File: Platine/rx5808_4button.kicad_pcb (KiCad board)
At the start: 2 copper layers, 50.5 x 29.5 mm, 52 parts, among them IC1 ATMEGA328-A, P1 CONN_01X02, P2 CONN_01X05, P5 BNC, P6 CONN_01X04, P7 CONN_02X05, U1 TPS62160, U2 RX5808, U3 sn74lvc1g3157, U4 MCPL3-BC-V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

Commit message: BOM für beide platinen des kompletten moduls dazugefügt
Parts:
- SMA_E1: footprint PhilippsFootprints:SMA_EDGE_small -> PhilippsFootprints:SMA_EDGE_Johnson_142-0701-801
- moved SMA_E1 2.20 mm to (106.7, 103.7)
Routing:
- net GND: track 187.9 -> 184.5 mm
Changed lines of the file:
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@@
     (thickness 1.6)
     (drawings 16)
-    (tracks 660)
+    (tracks 658)
     (zones 0)
     (modules 52)
@@
   )
   (setup
-    (last_trace_width 0.25)
+    (last_trace_width 0.254)
     (user_trace_width 0.2032)
     (user_trace_width 0.254)
@@
     (visible_elements FFFEFF39)
     (pcbplotparams
-      (layerselection 0x014f0_ffffffff)
+      (layerselection 0x010f0_ffffffff)
       (usegerberextensions true)
       (excludeedgelayer true)
@@
       (plotinvisibletext false)
       (padsonsilk false)
-      (subtractmaskfromsilk false)
+      (subtractmaskfromsilk true)
       (outputformat 1)
       (mirror false)
@@
     )
   )
-  (module PhilippsFootprints:SMA_EDGE_small (layer F.Cu)
-    (at 106.7 105.9 180)
-    (fp_text reference SMA_E1 (at 0 0 180) (layer F.SilkS)
-      (effects (font (thickness 0.3048)))
-    )
-    (fp_text value SMA_EDGE (at 0 2.54 180) (layer F.SilkS) hide
-      (effects (font (thickness 0.3048)))
-    )
-    (fp_line (start -6.35 -2.5654) (end -6.35 5.0546) (layer F.SilkS) (width 0.381))
-    (fp_line (start -6.35 5.0546) (end 6.35 5.0546) (layer F.SilkS) (width 0.381))
-    (fp_line (start 6.35 5.0546) (end 6.35 -2.5654) (layer F.SilkS) (width 0.381))
-    (fp_line (start 6.35 -2.5654) (end -6.35 -2.5654) (layer F.SilkS) (width 0.381))
-    (pad 0 connect rect (at -8.8773 -1.89484 180) (size 4.572 1.524) (layers *.Cu F.Mask)
-      (net 2 GND))
-    (pad 1 connect trapezoid (at -6.858 1.27 180) (size 0.50038 1.39954) (rect_delta 0.59944 0 ) (layers B.Cu B.Mask)
-      (net 27 "Net-(SMA_E1-Pad1)"))
-    (pad 2 connect rect (at -8.8773 4.42976 180) (size 4.572 1.524) (layers *.Cu F.Mask)
-      (net 2 GND))
-    (pad 1 connect rect (at -9.144 1.27 180) (size 4.07162 1.99898) (layers B.Cu B.Mask)
-      (net 27 "Net-(SMA_E1-Pad1)") (clearance 0.5))
-    (model SMA_EDGE.wrl
-      (at (xyz -0.205 -0.05 -0.12))
-      (scale (xyz 1.3 1.3 1.3))
-      (rotate (xyz 270 0 180))
-    )
-  )
   (module NR3015:NR3015 (layer F.Cu)
     (at 129.4 117.6 90)
@@
     )
   )
+  (module PhilippsFootprints:SMA_EDGE_Johnson_142-0701-801 (layer F.Cu)
+    (at 106.7 103.7 180)
+    (fp_text reference SMA_E1 (at 0 -1.3 180) (layer F.SilkS)
+      (effects (font (thickness 0.3048)))
+    )
+    (fp_text value SMA_EDGE (at 0 1.24 180) (layer F.SilkS) hide
+      (effects (font (thickness 0.3048)))
+    )
+    (fp_line (start -6.2 -5.6) (end -6.3 -5.6) (layer F.SilkS) (width 0.15))
+    (fp_line (start -6.3 -5.6) (end -11.2 -5.6) (layer F.SilkS) (width 0.15))
+    (fp_line (start -11.2 -5.6) (end -11.2 5.6) (layer F.SilkS) (width 0.15))
+    (fp_line (start -11.2 5.6) (end -6.2 5.6) (layer F.SilkS) (width 0.15))
+    (fp_line (start -6.2 5.6) (end -6.2 -5.6) (layer F.SilkS) (width 0.15))
+    (fp_line (start -6.35 -3.8654) (end -6.35 3.7546) (layer F.SilkS) (width 0.381))
+    (fp_line (start -6.35 3.7546) (end 6.35 3.7546) (layer F.SilkS) (width 0.381))
+    (fp_line (start 6.35 3.7546) (end 6.35 -3.8654) (layer F.SilkS) (width 0.381))
+    (fp_line (start 6.35 -3.8654) (end -6.35 -3.8654) (layer F.SilkS) (width 0.381))
+    (pad 0 connect rect (at -8.9 -4.4 180) (size 4.572 2.413) (layers *.Mask B.Cu)
+      (net 2 GND))
+    (pad 1 connect trapezoid (at -6.858 -0.03 180) (size 0.50038 1.39954) (rect_delta 0.59944 0 ) (layers B.Cu B.Mask)
+      (net 27 "Net-(SMA_E1-Pad1)"))
+    (pad 2 connect rect (at -8.9 4.4 180) (size 4.572 2.413) (layers *.Mask B.Cu)
+      (net 2 GND))
+    (pad 1 connect rect (at -9.144 -0.03 180) (size 4.07162 2.2) (layers B.Cu B.Mask)
+      (net 27 "Net-(SMA_E1-Pad1)"))
+    (model SMA_EDGE.wrl
+      (at (xyz -0.205 -0.05 -0.12))
+      (scale (xyz 1.3 1.3 1.3))
+      (rotate (xyz 270 0 180))
+    )
+  )
   (gr_text 12V (at 118.7 116.8 90) (layer F.SilkS)
     (effects (font (size 1.5 1.5) (thickness 0.3)))
   )
-  (gr_text Antenne (at 119.7 104.7) (layer F.SilkS)
+  (gr_text Antenne (at 105.4 110.8) (layer F.SilkS)
     (effects (font (size 1.5 1.5) (thickness 0.3)))
   )
@@
   (segment (start 142.525 99.7) (end 141.61381 98.78881) (width 0.254) (layer F.Cu) (net 1) (status 10))
   (segment (start 142.55 99.7) (end 142.525 99.7) (width 0.254) (layer F.Cu) (net 1) (status 30))
+  (segment (start 121.26 107.17) (end 121.26 107.54) (width 1.016) (layer B.Cu) (net 2))
+  (segment (start 121.26 107.54) (end 120.7 108.1) (width 1.016) (layer B.Cu) (net 2))
+  (segment (start 120.7 108.1) (end 115.6 108.1) (width 1.016) (layer B.Cu) (net 2))
+  (segment (start 121.26 102.09) (end 121.26 100.96) (width 1.016) (layer B.Cu) (net 2))
+  (segment (start 119.6 99.3) (end 115.6 99.3) (width 1.016) (layer B.Cu) (net 2))
+  (segment (start 121.26 100.96) (end 119.6 99.3) (width 1.016) (layer B.Cu) (net 2))
   (segment (start 127.5 101.2) (end 127.5 99.84) (width 0.4064) (layer F.Cu) (net 2))
   (segment (start 127.5 99.84) (end 128.54 98.8) (width 0.4064) (layer F.Cu) (net 2))
-  (segment (start 115.5773 107.79484) (end 118.20516 107.79484) (width 0.254) (layer B.Cu) (net 2))
-  (segment (start 118.20516 107.79484) (end 118.32024 107.67976) (width 0.254) (layer B.Cu) (net 2))
-  (segment (start 115.5773 101.47024) (end 117.99008 101.47024) (width 0.254) (layer B.Cu) (net 2))
-  (segment (start 117.99008 101.47024) (end 118.10516 101.35516) (width 0.254) (layer B.Cu) (net 2))
   (segment (start 128.54 98.8) (end 130.08778 100.34778) (width 0.4064) (layer B.Cu) (net 2))
   (segment (start 130.08778 100.34778) (end 134.31774 100.34778) (width 0.4064) (layer B.Cu) (net 2))
@@
   (segment (start 144.3 117.74996) (end 144.3 120.4) (width 0.254) (layer F.Cu) (net 2) (status 30))
   (segment (start 144.3 120.4) (end 144.4 120.5) (width 0.254) (layer F.Cu) (net 2) (status 30))
-  (segment (start 115.6273 101.35516) (end 118.10516 101.35516) (width 1.016) (layer B.Cu) (net 2) (status 10))
-  (segment (start 118.84 102.09) (end 121.26 102.09) (width 1.016) (layer B.Cu) (net 2) (status 20))
-  (segment (start 118.10516 101.35516) (end 118.84 102.09) (width 1.016) (layer B.Cu) (net 2))
-  (segment (start 121.26 107.17) (end 118.83 107.17) (width 1.016) (layer B.Cu) (net 2) (status 10))
-  (segment (start 118.32024 107.67976) (end 115.6273 107.67976) (width 1.016) (layer B.Cu) (net 2) (status 20))
-  (segment (start 118.83 107.17) (end 118.32024 107.67976) (width 1.016) (layer B.Cu) (net 2))
   (segment (start 145.537717 117.023276) (end 147 118.485559) (width 0.254) (layer F.Cu) (net 2) (status 20))
   (segment (start 147 118.485559) (end 147 118.55) (width 0.254) (layer F.Cu) (net 2) (status 30))
@@
   (segment (start 127.05 120.6) (end 127.05 121.65) (width 0.254) (layer F.Cu) (net 26) (status 20))
   (segment (start 127 119.975) (end 127 120.55) (width 0.254) (layer F.Cu) (net 26) (status 10))
-  (segment (start 121.26 104.63) (end 115.844 104.63) (width 1.016) (layer B.Cu) (net 27))
-  (segment (start 115.844 104.63) (end 113.558 104.63) (width 0.254) (layer B.Cu) (net 27))
+  (segment (start 113.558 103.73) (end 115.844 103.73) (width 0.254) (layer B.Cu) (net 27))
+  (segment (start 121.26 104.63) (end 119.23 104.63) (width 1.016) (layer B.Cu) (net 27))
+  (segment (start 118.33 103.73) (end 115.844 103.73) (width 1.016) (layer B.Cu) (net 27))
+  (segment (start 119.23 104.63) (end 118.33 103.73) (width 1.016) (layer B.Cu) (net 27))
   (segment (start 121.16516 104.53516) (end 121.26 104.63) (width 0.254) (layer B.Cu) (net 27) (status 30))
   (segment (start 121.15 104.52) (end 121.26 104.63) (width 0.508) (layer B.Cu) (net 27) (status 30))

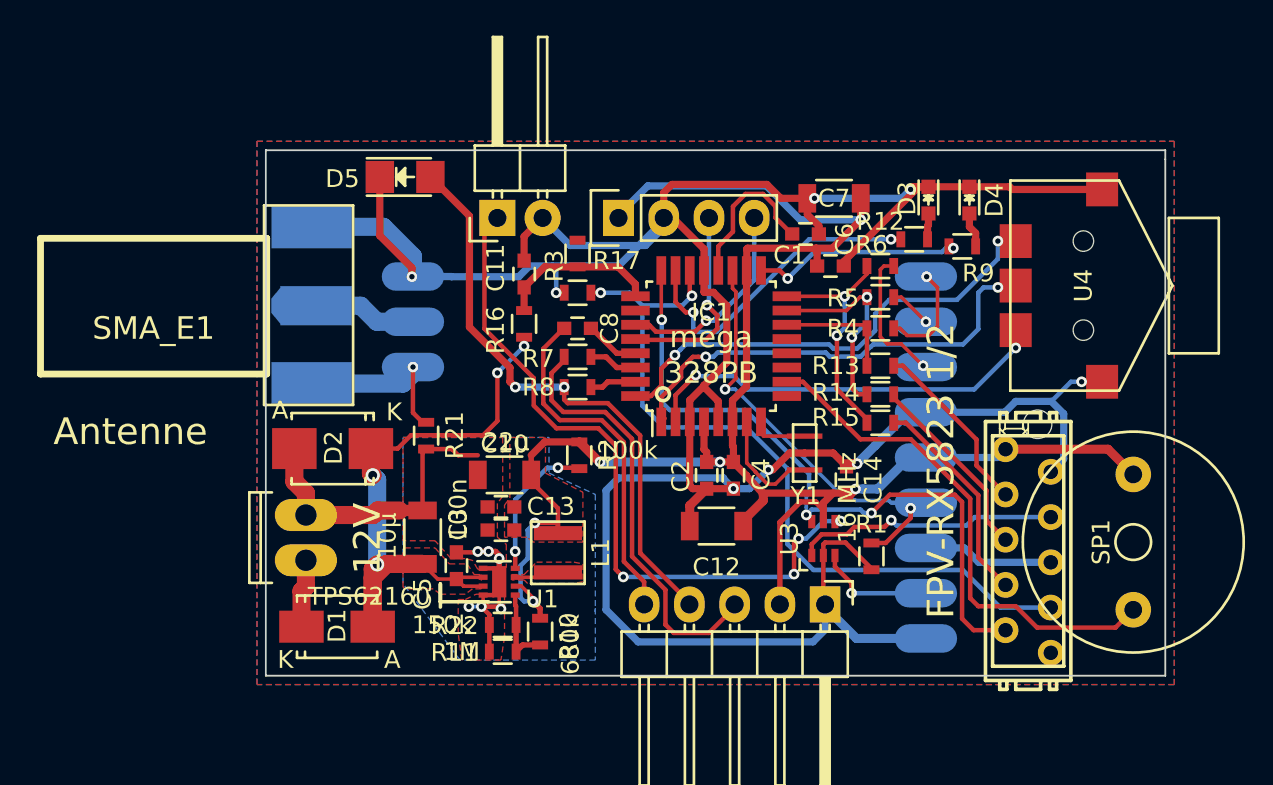
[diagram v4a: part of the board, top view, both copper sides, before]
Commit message: jetzt auch layout geändert. micromatchbuchse und/oder buzzer sollten noch verschoben werden!
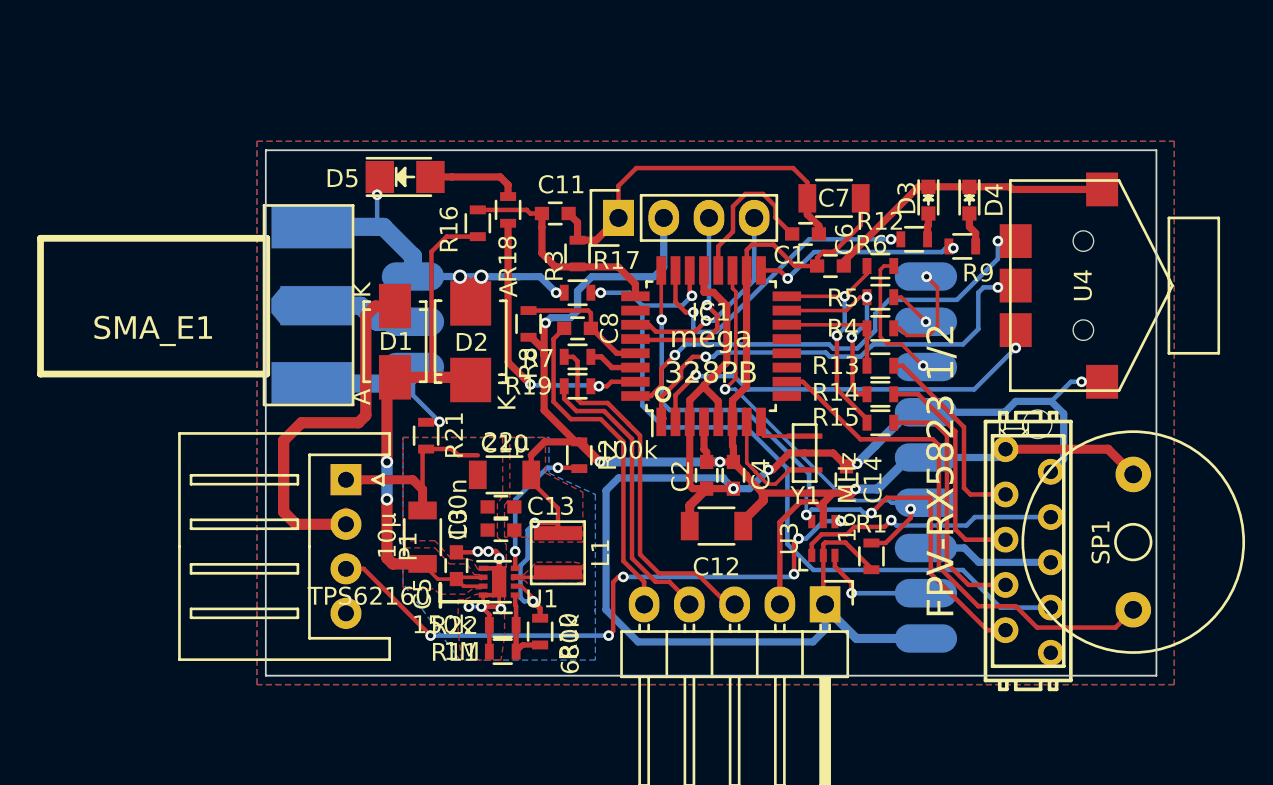
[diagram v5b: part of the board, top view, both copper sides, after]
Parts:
- removed P5: BNC, Pin_Headers:Pin_Header_Angled_1x02
- added R18: 100, Resistors_SMD:R_0603, F.Cu at (126.6, 98.3)
- added R19: 1k, Resistors_SMD:R_0603, F.Cu at (130.5, 108.2)
- P1: value CONN_01X02 -> CONN_01X04; footprint Sockets_MOLEX_KK-System:Socket_MOLEX-KK-RM2-54mm_Lock_2pin_straight -> Connectors_JST:JST_XH_S04B-XH-A_04x2.50mm_Angled
- R1, R3: value 1M -> 100k
- R8: value 220 -> 10k
- moved D1 16.3 mm to (120.2, 105.8), turned to 270 degrees
- moved D2 9.80 mm to (124.5, 105.8), turned to 90 degrees
- moved R16 6.22 mm to (124.9, 99.1)
- moved R8 4.49 mm to (127.8, 104.8), turned to 90 degrees
- moved P1 3.95 mm to (117.5, 113.5), turned to 270 degrees
- moved C11 3.82 mm to (129.2, 98.5), turned to 0 degrees
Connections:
- D2 pad 2: GNDPWR -> GND
- D5 pad 2: /txd -> Net-(D5-Pad2)
- P1 pad 1: Net-(D1-Pad1) -> GNDPWR
- P1 pad 2: GNDPWR -> Net-(D1-Pad1)
- P6 pad 1: +5V -> GND
- P6 pad 2: GND -> +5V
- R8 pad 1: /txd -> +5V
- R8 pad 2: Net-(IC1-Pad31) -> /reset
- U3 pad 4: Net-(P5-Pad1) -> /VidOut
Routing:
- net Net-(P5-Pad1): track 39.9 -> 0.00 mm, vias 4 -> 0
- net /VidOut: track 0.00 -> 34.9 mm, vias 0 -> 6
- net GND: track 184.5 -> 163.0 mm
- net Net-(D1-Pad1): track 3.83 -> 21.1 mm
- net /txd: track 33.7 -> 17.4 mm, vias 2 -> 0
- net Net-(IC1-Pad31): track 2.62 -> 16.5 mm, vias 0 -> 2
- net +5V: track 106.4 -> 112.4 mm
- net +12V: track 37.6 -> 32.2 mm, vias 4 -> 2
- net Net-(D5-Pad2): track 0.00 -> 5.20 mm
- net GNDPWR: track 31.7 -> 26.7 mm
- net /reset: track 3.08 -> 7.49 mm
- net /adc_12V: track 9.11 -> 12.6 mm
- net /rxd: track 24.5 -> 21.1 mm
- net /Funk2_clk: track 12.1 -> 14.3 mm
- net /Funk2_ss: track 10.8 -> 12.9 mm
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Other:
- board size 50.5 x 29.5 mm -> 50 x 29.5 mm
- rule trace_min: 0.15 -> 0.155
- board text removed: "12V"
- board text removed: "Antenne"

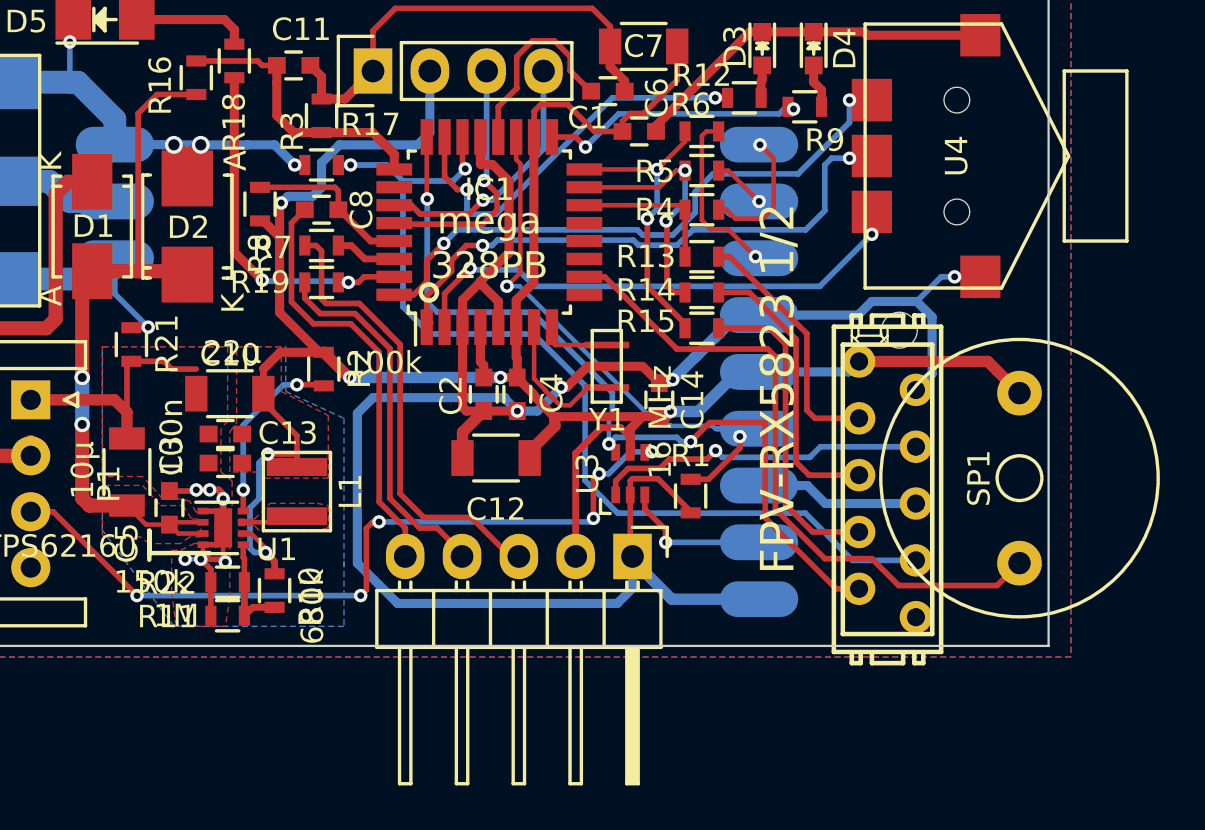
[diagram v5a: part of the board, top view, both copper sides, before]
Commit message: fuses-datei für den Atmega328PB dazugefügt, Bootloaderstecker auf JST PH geändert, Filterkondensator und Widerstand für OLED hinzugefügt
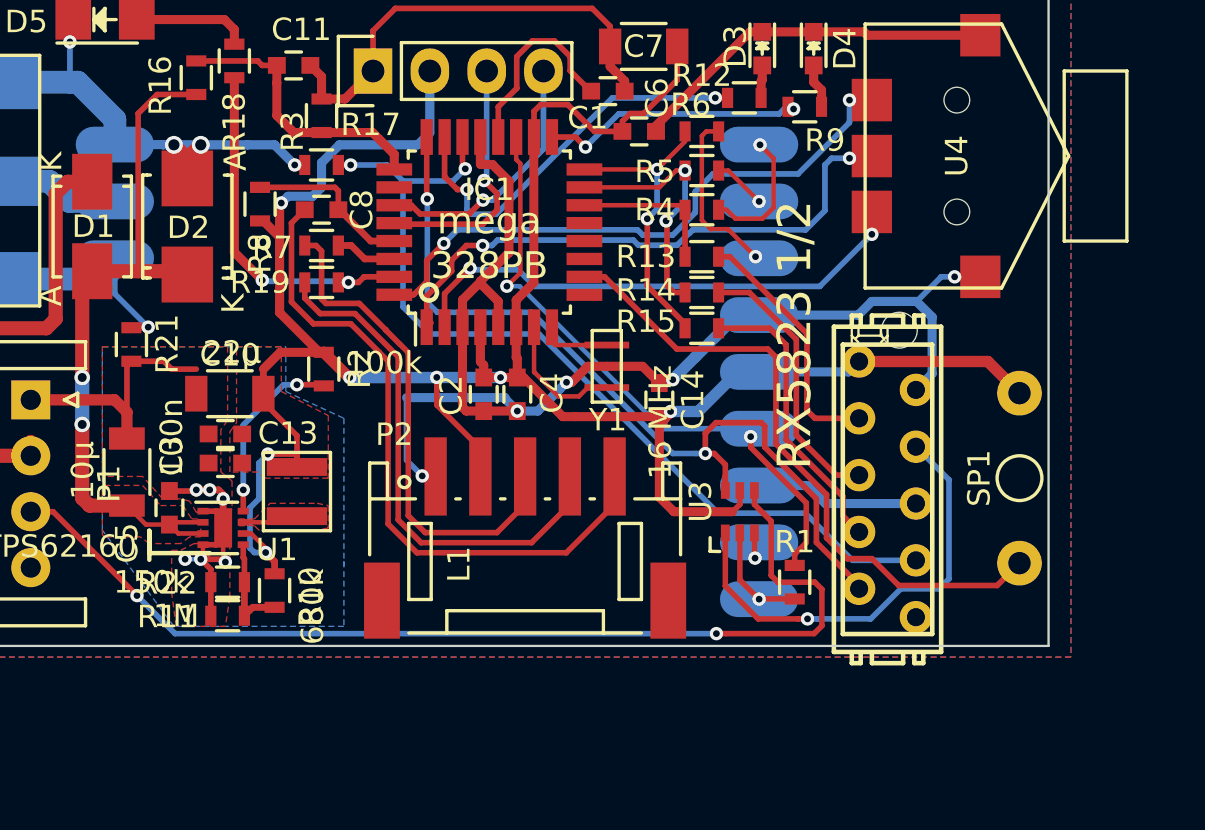
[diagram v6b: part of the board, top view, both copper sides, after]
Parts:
- removed C12: 22µ, Capacitors_SMD:C_1206
- P2: footprint Pin_Headers:Pin_Header_Angled_1x05 -> Connectors_JST:JST_PH_S5B-PH-SM4-TB_05x2.00mm_Angled
- moved R1 6.04 mm to (151.7, 121.7)
- moved U3 5.19 mm to (149.2, 118.5)
- moved P2 4.87 mm to (139.6, 119.7), turned to 0 degrees
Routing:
- net GND: track 163.0 -> 132.5 mm, vias 9 -> 11
- net /VidOut: track 34.9 -> 46.0 mm, vias 6 -> 2
- net /DTR: track 19.7 -> 29.9 mm
- net /txd: track 17.4 -> 23.3 mm
- net /Video2: track 14.9 -> 20.2 mm
- net /Video1: track 6.68 -> 1.92 mm
- net /rssi1: track 25.4 -> 29.6 mm
- net /rssi2: track 43.4 -> 40.9 mm
- net /rxd: track 21.1 -> 22.7 mm
- net /Funk2_clk: track 14.3 -> 13.0 mm
- net +5V: track 112.4 -> 113.4 mm, vias 6 -> 7
- net /led2: track 37.5 -> 38.4 mm, vias 3 -> 2
- net /Funk2_ss: track 12.9 -> 12.2 mm
- net /buzzer: track 29.6 -> 29.0 mm
- net Net-(IC1-Pad7): track 6.39 -> 5.87 mm
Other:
- rule pad_to_mask_clearance: 0.15 -> 0.1
- board text added: "RX5823 1/2"
- board text removed: "FPV-RX5823 1/2"
